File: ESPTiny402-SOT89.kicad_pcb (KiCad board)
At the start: 2 copper layers, 26.4 x 23.9 mm, 20 parts, among them J1 Conn_01x10_Male, J2 Conn_01x10_Male, J3 Conn_01x04_Male, U1 ESP-01v090, U2 ATtiny402-SS, U3 MCP1700

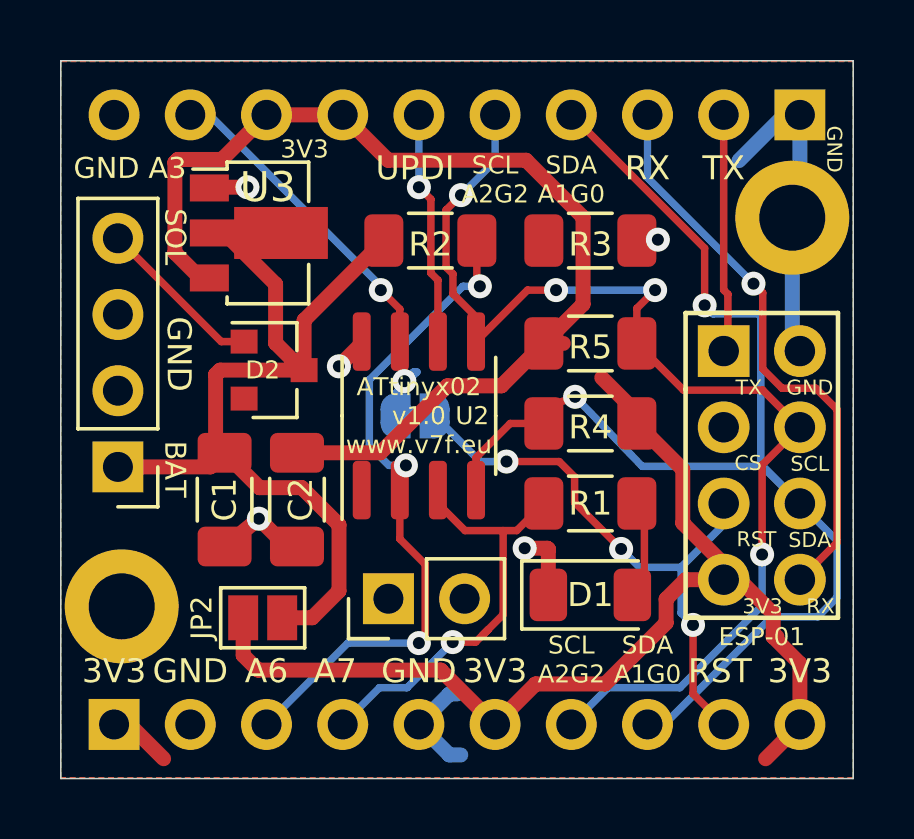
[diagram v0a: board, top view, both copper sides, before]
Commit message: Minor cosmetic cleanups
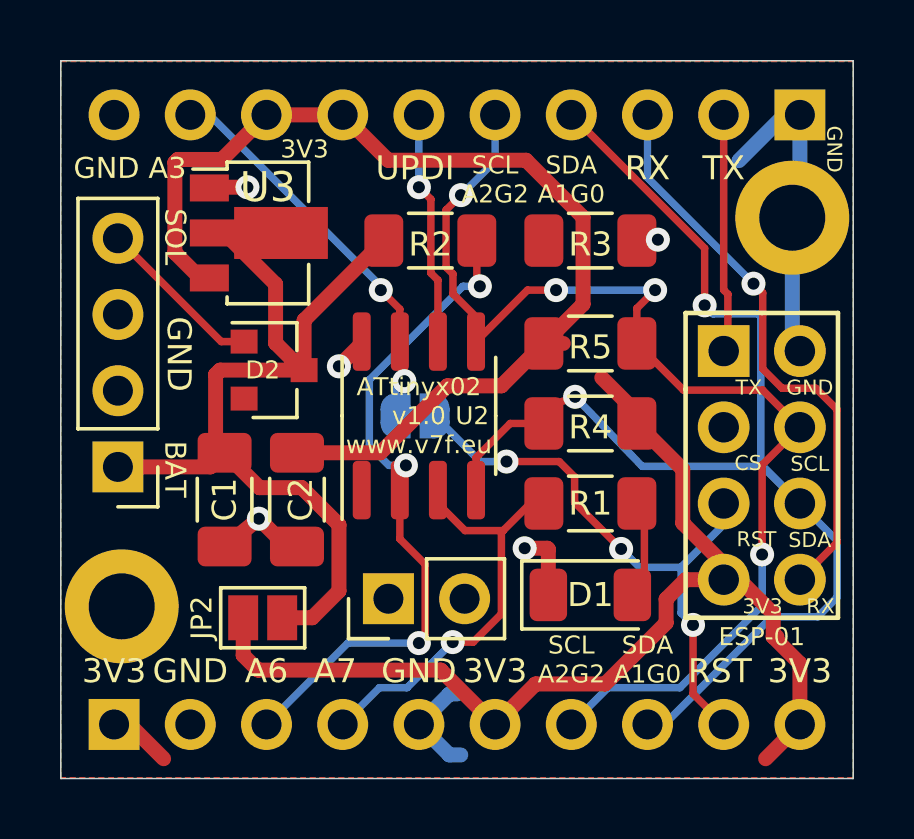
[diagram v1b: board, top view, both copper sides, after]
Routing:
- net /A7: track 15.4 -> 14.3 mm
- net /A3: track 14.5 -> 13.5 mm
- net /UPDI: track 8.50 -> 7.82 mm
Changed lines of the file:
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@@
 		(0 "F.Cu" signal)
 		(2 "B.Cu" signal)
-		(9 "F.Adhes" user)
-		(11 "B.Adhes" user)
+		(9 "F.Adhes" user "F.Adhesive")
+		(11 "B.Adhes" user "B.Adhesive")
 		(13 "F.Paste" user)
 		(15 "B.Paste" user)
-		(5 "F.SilkS" user)
-		(7 "B.SilkS" user)
+		(5 "F.SilkS" user "F.Silkscreen")
+		(7 "B.SilkS" user "B.Silkscreen")
 		(1 "F.Mask" user)
 		(3 "B.Mask" user)
-		(17 "Dwgs.User" user)
-		(19 "Cmts.User" user)
-		(21 "Eco1.User" user)
-		(23 "Eco2.User" user)
+		(17 "Dwgs.User" user "User.Drawings")
+		(19 "Cmts.User" user "User.Comments")
+		(21 "Eco1.User" user "User.Eco1")
+		(23 "Eco2.User" user "User.Eco2")
 		(25 "Edge.Cuts" user)
 		(27 "Margin" user)
-		(31 "F.CrtYd" user)
-		(29 "B.CrtYd" user)
+		(31 "F.CrtYd" user "F.Courtyard")
+		(29 "B.CrtYd" user "B.Courtyard")
 		(35 "F.Fab" user)
 		(33 "B.Fab" user)
@@
 	)
 	(segment
-		(start 61.973 56.645)
-		(end 61.976 56.642)
-		(width 0.5)
-		(layer "F.Cu")
-		(net 1)
-	)
-	(segment
 		(start 50.675 44.577)
 		(end 51.943 44.577)
@@
 	)
 	(segment
-		(start 59.195532 56.02201)
-		(end 58.293 55.119478)
-		(width 0.25)
-		(layer "F.Cu")
-		(net 6)
-	)
-	(segment
-		(start 59.961501 59.326501)
-		(end 60.46701 58.820992)
-		(width 0.25)
-		(layer "F.Cu")
-		(net 6)
-	)
-	(segment
 		(start 58.785225 59.739574)
-		(end 59.548428 59.739574)
+		(end 59.469252 59.739574)
 		(width 0.25)
 		(layer "F.Cu")
@@
 	)
 	(segment
-		(start 61.823 55.118)
-		(end 60.91899 56.02201)
+		(start 59.195532 56.02201)
+		(end 58.293 55.119478)
 		(width 0.25)
 		(layer "F.Cu")
@@
 	)
 	(segment
-		(start 60.91899 56.02201)
+		(start 60.40752 56.0815)
 		(end 60.46701 56.02201)
 		(width 0.25)
@@
 	)
 	(segment
-		(start 59.770001 59.518001)
-		(end 59.961501 59.326501)
+		(start 61.37102 55.118)
+		(end 61.823 55.118)
 		(width 0.25)
 		(layer "F.Cu")
@@
 	)
 	(segment
-		(start 59.548428 59.739574)
-		(end 59.961501 59.326501)
+		(start 60.40752 58.761502)
+		(end 60.40752 56.0815)
 		(width 0.25)
 		(layer "F.Cu")
@@
 	)
 	(segment
-		(start 55.118 62.484)
-		(end 55.844998 62.484)
+		(start 60.46701 56.02201)
+		(end 61.37102 55.118)
 		(width 0.25)
 		(layer "F.Cu")
@@
 	)
 	(segment
-		(start 60.46701 58.820992)
-		(end 60.46701 56.02201)
+		(start 59.469252 59.739574)
+		(end 60.408 58.800826)
 		(width 0.25)
 		(layer "F.Cu")
@@
 	)
 	(segment
-		(start 56.881 51.449408)
-		(end 56.881 52.197)
+		(start 56.881 52.197)
+		(end 56.881 51.333366)
 		(width 0.25)
 		(layer "B.Cu")
@@
 	)
 	(segment
-		(start 57.478162 50.736204)
+		(start 56.881 51.333366)
 		(end 57.173498 51.040868)
 		(width 0.25)
@@
 	)
 	(segment
-		(start 57.594204 50.736204)
-		(end 56.881 51.449408)
-		(width 0.25)
-		(layer "B.Cu")
-		(net 10)
-	)
-	(segment
-		(start 57.594204 50.736204)
-		(end 57.478162 50.736204)
-		(width 0.25)
-		(layer "B.Cu")
-		(net 10)
-	)
-	(segment
 		(start 57.023 54.672)
 		(end 57.023 56.298998)
@@
 	)
 	(segment
-		(start 57.023 55.119478)
-		(end 57.023 54.672)
-		(width 0.25)
-		(layer "F.Cu")
-		(net 12)
-	)
-	(segment
 		(start 59.589 46.355)
 		(end 59.589 47.778)
@@
 		(width 0.25)
 		(layer "F.Cu")
-		(net 15)
-	)
-	(segment
-		(start 57.658 42.164)
-		(end 58.014021 42.520021)
-		(width 0.25)
-		(layer "F.Cu")
-		(net 15)
-	)
-	(segment
-		(start 58.293 49.722)
-		(end 58.118 49.722)
-		(width 0.25)
-		(layer "F.Cu")
